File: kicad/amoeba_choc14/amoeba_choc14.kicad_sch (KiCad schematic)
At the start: 6 parts, among them J1 Conn_01x01_Pin, J2 Conn_01x01_Pin, J3 Conn_01x01_Pin, J4 Conn_01x01_Pin, SW1 SW_SPST

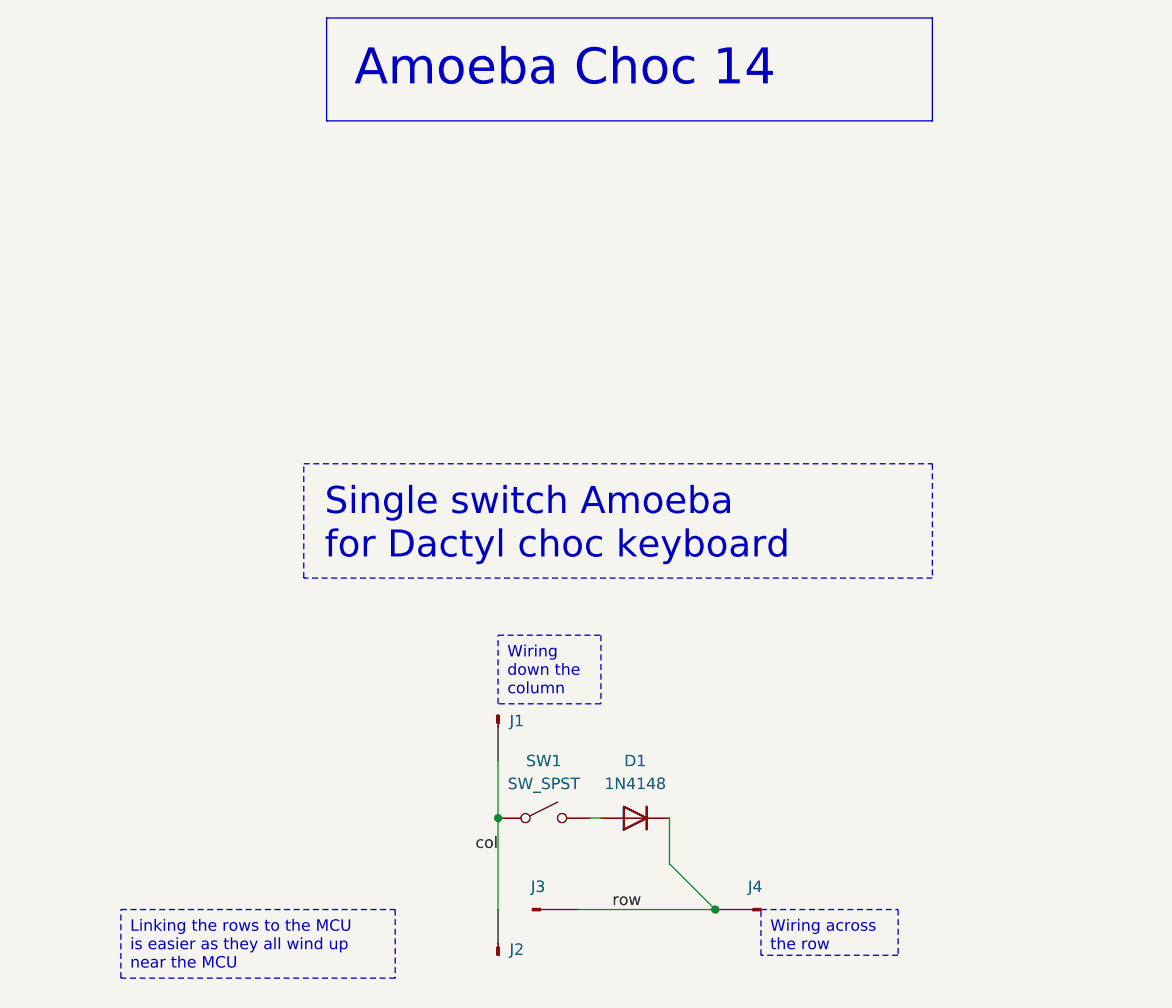
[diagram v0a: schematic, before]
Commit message: feat(amoeba): bump version, straighten trace
-   update to KiCad 9
-   increase font size in schematic
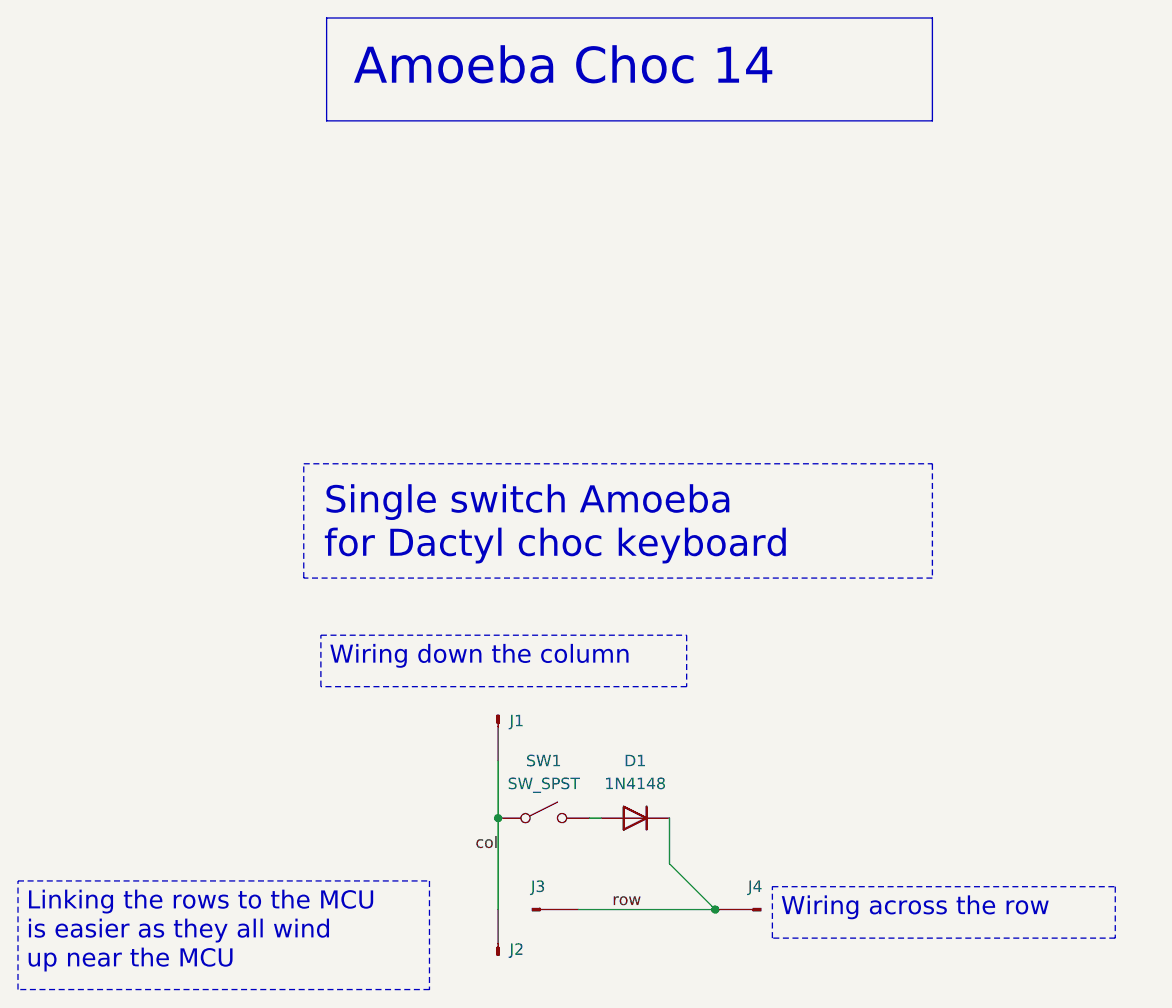
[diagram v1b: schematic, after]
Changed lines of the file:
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@@
 (kicad_sch
-	(version 20231120)
+	(version 20250114)
 	(generator "eeschema")
-	(generator_version "8.0")
+	(generator_version "9.0")
 	(paper "USLetter")
 	(title_block
 		(title "Amoeba Choc 14")
-		(date "2024-08-21")
-		(rev "0.1.0-alpha.2")
+		(date "2025-03-30")
+		(rev "0.1.0-alpha.3")
 		(comment 3 "A choc keyboard single-switch Amoeba PCB with Mill-Max hotswap")
+	)
+	(text_box "${TITLE}"
+		(exclude_from_sim no)
+		(at 105.41 13.97 0)
+		(size 67.31 11.43)
+		(margins 3 3 3 3)
+		(stroke
+			(width 0)
+			(type default)
+		)
+		(fill
+			(type none)
+		)
+		(effects
+			(font
+				(size 4 4)
+			)
+			(justify left top)
+		)
+	)
+	(text_box "Linking the rows to the MCU\nis easier as they all wind up near the MCU"
+		(exclude_from_sim no)
+		(at 71.12 109.855 0)
+		(size 45.72 12.065)
+		(margins 0.9525 0.9525 0.9525 0.9525)
+		(stroke
+			(width 0)
+			(type dot)
+		)
+		(fill
+			(type none)
+		)
+		(effects
+			(font
+				(size 2 2)
+			)
+			(justify left top)
+		)
+	)
+	(text_box "Single switch Amoeba\nfor Dactyl choc keyboard"
+		(exclude_from_sim no)
+		(at 102.87 63.5 0)
+		(size 69.85 12.7)
+		(margins 2.25 2.25 2.25 2.25)
+		(stroke
+			(width 0)
+			(type dash)
+		)
+		(fill
+			(type none)
+		)
+		(effects
+			(font
+				(size 3 3)
+			)
+			(justify left top)
+		)
+	)
+	(text_box "Wiring down the column"
+		(exclude_from_sim no)
+		(at 104.775 82.55 0)
+		(size 40.64 5.715)
+		(margins 0.9525 0.9525 0.9525 0.9525)
+		(stroke
+			(width 0)
+			(type dot)
+		)
+		(fill
+			(type none)
+		)
+		(effects
+			(font
+				(size 2 2)
+			)
+			(justify left top)
+		)
+	)
+	(text_box "Wiring across the row"
+		(exclude_from_sim no)
+		(at 154.94 110.49 0)
+		(size 38.1 5.715)
+		(margins 0.9525 0.9525 0.9525 0.9525)
+		(stroke
+			(width 0)
+			(type dot)
+		)
+		(fill
+			(type none)
+		)
+		(effects
+			(font
+				(size 2 2)
+			)
+			(justify left top)
+		)
 	)
 	(junction
@@
 		)
 	)
-	(text_box "${TITLE}"
-		(exclude_from_sim no)
-		(at 105.41 13.97 0)
-		(size 67.31 11.43)
-		(stroke
-			(width 0)
-			(type default)
-		)
-		(fill
-			(type none)
-		)
-		(effects
-			(font
-				(size 4 4)
-			)
-			(justify left top)
-		)
-	)
-	(text_box "Linking the rows to the MCU\nis easier as they all wind up near the MCU"
-		(exclude_from_sim no)
-		(at 82.55 113.03 0)
-		(size 30.48 7.62)
-		(stroke
-			(width 0)
-			(type dot)
-		)
-		(fill
-			(type none)
-		)
+	(label "col"
+		(at 124.46 106.68 180)
 		(effects
 			(font
 				(size 1.27 1.27)
 			)
-			(justify left top)
-		)
-	)
-	(text_box "Single switch Amoeba\nfor Dactyl choc keyboard"
-		(exclude_from_sim no)
-		(at 102.87 63.5 0)
-		(size 69.85 12.7)
-		(stroke
-			(width 0)
-			(type dash)
-		)
-		(fill
-			(type none)
-		)
-		(effects
-			(font
-				(size 3 3)
-			)
-			(justify left top)
-		)
-	)
-	(text_box "Wiring down the column"
-		(exclude_from_sim no)
-		(at 124.46 82.55 0)
-		(size 11.43 7.62)
-		(stroke
-			(width 0)
-			(type dot)
-		)
-		(fill
-			(type none)
-		)
-		(effects
-			(font
-				(size 1.27 1.27)
-			)
-			(justify left top)
-		)
-	)
-	(text_box "Wiring across the row"
-		(exclude_from_sim no)
-		(at 153.67 113.03 0)
-		(size 15.24 5.08)
-		(stroke
-			(width 0)
-			(type dot)
-		)
-		(fill
-			(type none)
-		)
-		(effects
-			(font
-				(size 1.27 1.27)
-			)
-			(justify left top)
-		)
-	)
-	(label "col"
-		(at 124.46 106.68 180)
-		(fields_autoplaced yes)
-		(effects
-			(font
-				(size 1.27 1.27)
-			)
 			(justify right bottom)
 		)
@@
 	(label "row"
 		(at 137.16 113.03 0)
-		(fields_autoplaced yes)
 		(effects
 			(font
@@
 		)
 	)
+	(embedded_fonts no)
 )

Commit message: feat(amoeba): SOD-123 diode, fewer silk tick marks
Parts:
- D1: footprint Diode_SMD:D_SOD-323_HandSoldering -> Diode_SMD:D_SOD-123; LCSC C2128 -> C81598
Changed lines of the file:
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@@
 	(title_block
 		(title "Amoeba Choc 14")
-		(date "2025-03-30")
-		(rev "0.1.0-alpha.3")
+		(date "2025-06-28")
+		(rev "0.1.0-alpha.4")
 		(comment 3 "A choc keyboard single-switch Amoeba PCB with Mill-Max hotswap")
 	)
@@
 			)
 		)
-		(property "Footprint" "Diode_SMD:D_SOD-323_HandSoldering"
+		(property "Footprint" "Diode_SMD:D_SOD-123"
 			(at 139.7 102.87 0)
 			(effects
@@
 			)
 		)
-		(property "LCSC" "C2128"
-			(at 139.7 102.87 0)
-			(effects
+		(property "LCSC" "C81598"
+			(at 139.7 102.87 0)
+			(effects
